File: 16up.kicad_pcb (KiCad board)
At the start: 2 copper layers, 60.8 x 85 mm, 20 parts, among them CN1 EXPANSION_PORT, CN2 ALMOST_USERPORT, CN4 TAPE_IN, J3 CONN_UPORT254, U1 GAL20V8, U102 74LS652, U2 MOS_6529, U3 MOS_6551_ACIA, U4 74HCT04, Y1 1.8432M

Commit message: Close #3
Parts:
- U102: value 74LS652 -> 74LS654
- renumbered J3 to CN3

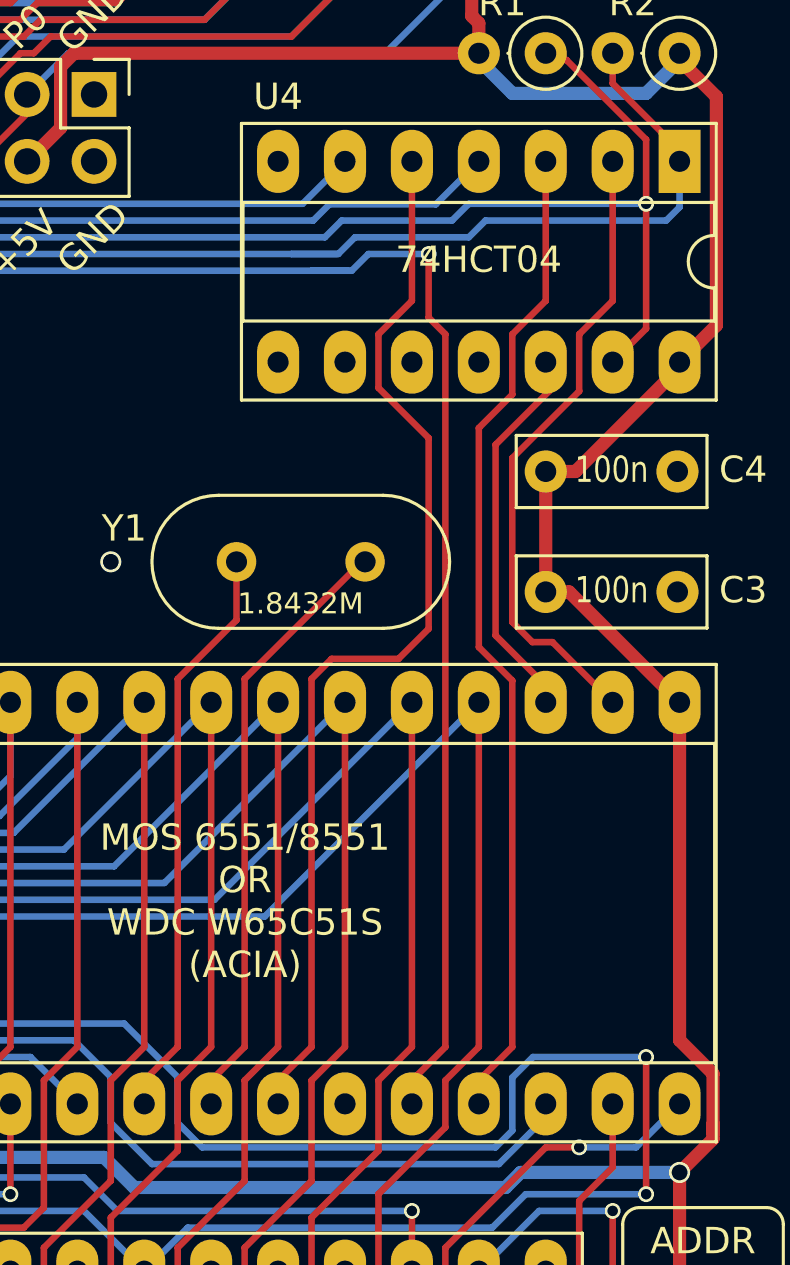
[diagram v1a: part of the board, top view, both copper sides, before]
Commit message: Add optional buffering for TX
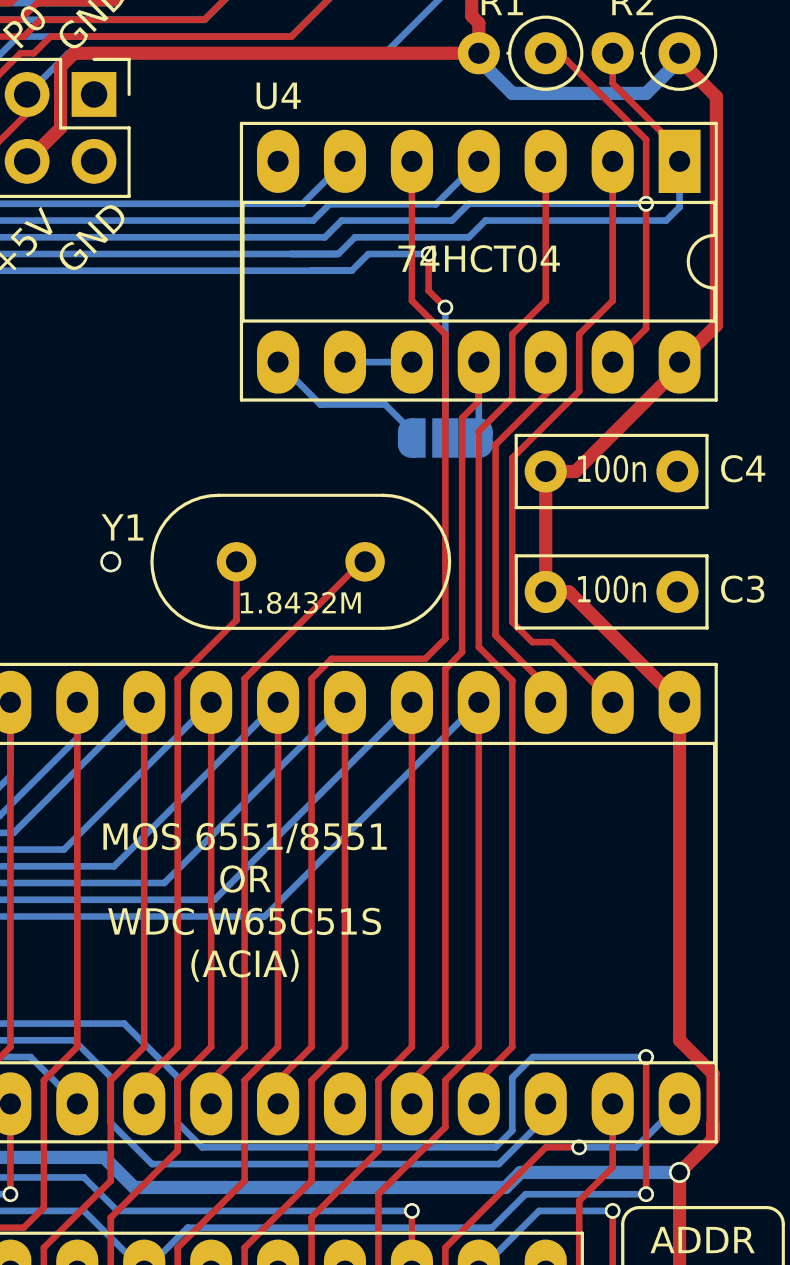
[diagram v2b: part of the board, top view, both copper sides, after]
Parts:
- added JP2: JMP_TXD_SEL, Jumper:SolderJumper-3_P1.3mm_Open_RoundedPad1.0x1.5mm, B.Cu at (169.0, 90.9)
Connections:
- CN2 pad M: /txd_ttl -> /txd_ttl_out
- CN3 pad 21: /txd_ttl -> /txd_ttl_out
- U4 pad 11: GND -> /txd_ttl
- U4 pad 9: GND -> Net-(U4-Pad10)
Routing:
- net /txd_ttl_out: track 0.00 -> 62.4 mm, vias 0 -> 2
- net /txd_ttl: track 88.2 -> 32.1 mm, vias 1 -> 0
- net Net-(JP2-Pad3): track 0.00 -> 6.41 mm
- net Net-(U4-Pad10): track 0.00 -> 2.54 mm
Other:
- board text added: "BUF"
- board text added: "V4"
- board text removed: "V3"
